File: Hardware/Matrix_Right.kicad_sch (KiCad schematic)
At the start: 125 parts, among them SW38 PG1350, SW39 PG1350, SW40 PG1350, SW41 PG1350, SW42 PG1350, SW43 PG1350, SW44 PG1350, SW45 PG1350, SW46 PG1350, SW47 PG1350, SW48 PG1350, SW49 PG1350, SW50 PG1350, SW51 PG1350, SW52 PG1350, SW53 PG1350, SW54 PG1350, SW55 PG1350, SW56 PG1350, SW57 PG1350, SW58 PG1350, SW59 PG1350, SW60 PG1350, SW61 PG1350, SW62 PG1350, SW63 PG1350, SW64 PG1350, SW65 PG1350, SW66 PG1350, SW67 PG1350, SW68 ENCODER

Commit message: MIP display and LED enable
Return of the LED enable via GPIO.
Changed the TFT display for a MPI panel. It's more expensive than an e-ink one, but the sharpness is really nice.
Need to remove the numbers row to go for a true Corne-ish layout.
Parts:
- renumbered C45 to C47, C46 to C48, C47 to C49, C48 to C50, C49 to C51, C50 to C52, C51 to C53, C52 to C54, C53 to C55, C54 to C56, C55 to C57, C56 to C58, C57 to C59, C58 to C60, C59 to C61, C60 to C62, C61 to C63, C62 to C64, C63 to C65, C64 to C66, C65 to C67, C66 to C68, C67 to C69, C68 to C70, C69 to C71, C70 to C72, C71 to C73, C72 to C74, C73 to C75, C74 to C76, C75 to C77, C76 to C78, D102 to D100, D103 to D101, D104 to D102, D105 to D103, D106 to D104, D107 to D105, D108 to D106, D109 to D107, D110 to D108, D111 to D109, D112 to D110, D113 to D111, D114 to D112, D115 to D113, D116 to D114, D117 to D115, D118 to D116, D119 to D117, D120 to D118, D121 to D119, D122 to D120, D123 to D121, D124 to D122, D125 to D123, D126 to D124, D67 to D65, D68 to D66, D69 to D67, D70 to D68, D71 to D69, D72 to D70, D73 to D71, D74 to D72, D75 to D73, D76 to D74, D77 to D75, D78 to D76, D79 to D77, D80 to D78, D81 to D79, D82 to D80, D83 to D81, D84 to D82, D85 to D83, D86 to D84, D87 to D85, D88 to D86, D89 to D87, D90 to D88, D91 to D89, D92 to D90, D93 to D91, D94 to D92, D95 to D93, D96 to D94, D97 to D95, D98 to D96, D99 to D97, D100 to D98, D101 to D99, R25 to R19, R26 to R20, SW38 to SW36, SW39 to SW37, SW40 to SW38, SW41 to SW39, SW42 to SW40, SW43 to SW41, SW44 to SW42, SW45 to SW43, SW46 to SW44, SW47 to SW45, SW48 to SW46, SW49 to SW47, SW50 to SW48, SW51 to SW49, SW52 to SW50, SW53 to SW51, SW54 to SW52, SW55 to SW53, SW56 to SW54, SW57 to SW55, SW58 to SW56, SW59 to SW57, SW60 to SW58, SW61 to SW59, SW62 to SW60, SW63 to SW61, SW64 to SW62, SW65 to SW63, SW66 to SW64, SW67 to SW65, SW68 to SW66

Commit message: Row removal and key layout
Removed the number row.
Adjusted the spacebar position and changed it to 1u.
Need to consider what to do for one of the halfs if its screen is to be removed.
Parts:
- removed C48, C51, C55, C59, C63, C67: 1u, Capacitor_SMD:C_0603_1608Metric, symbol Device:C
- removed D105, D114, D71, D80, D89, D98: 1N4148WT, Diode_SMD:D_SOD-523, symbol Diode:1N4148WT
- removed D110, D66, D69, D78, D87, D96: SK6812MINI-E, Custom_Parts:LED_SK6812MINI-E_3.2x2.8mm_P1.5mm_ReverseMount, symbol LED:SK6812MINI-E
- removed SW36, SW41, SW46, SW51, SW56, SW61: PG1350, Custom_Parts:PG1350_1.00u_PCB, symbol Switch:SW_Push
- renumbered C76 to C41, C73 to C42, C74 to C43, C72 to C44, C69 to C45, C70 to C46, C68 to C47, C65 to C48, C66 to C49, C64 to C50, C61 to C51, C62 to C52, C60 to C53, C57 to C54, C58 to C55, C53 to C57, C54 to C58, C52 to C59, C49 to C60, C50 to C61, C75 to C62, C71 to C63, C47 to C64, C77 to C65, C78 to C66, D65 to D100, D124 to D53, D121 to D54, D122 to D55, D120 to D56, D112 to D57, D113 to D58, D72 to D59, D73 to D60, D74 to D61, D75 to D62, D111 to D63, D103 to D64, D104 to D65, D81 to D66, D82 to D67, D83 to D68, D84 to D69, D97 to D70, D94 to D71, D95 to D72, D90 to D73, D91 to D74, D92 to D75, D93 to D76, D88 to D77, D99 to D78, D100 to D79, D101 to D80, D102 to D81, D85 to D82, D86 to D83, D79 to D84, D106 to D85, D107 to D86, D108 to D87, D109 to D88, D76 to D89, D77 to D90, D70 to D91, D115 to D92, D116 to D93, D117 to D94, D118 to D95, D67 to D96, D68 to D97, D123 to D98, D119 to D99, SW37 to SW30, SW38 to SW31, SW39 to SW32, SW40 to SW33, SW42 to SW34, SW43 to SW35, SW44 to SW36, SW45 to SW37, SW47 to SW38, SW48 to SW39, SW49 to SW40, SW50 to SW41, SW52 to SW42, SW53 to SW43, SW54 to SW44, SW55 to SW45, SW57 to SW46, SW58 to SW47, SW59 to SW48, SW60 to SW49, SW62 to SW50, SW63 to SW51, SW64 to SW52, SW65 to SW53, SW66 to SW54
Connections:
- net ROW5_R is gone; now on net ROW4_R: D62.1 (K), D69.1 (K), D76.1 (K), D81.1 (K), D88.1 (K), D95.1 (K)
- net LED_DATA_R: now also D54.2 (DIN)
- net ROW1_R: now also D59.1 (K), D66.1 (K), D73.1 (K), D78.1 (K), D85.1 (K), D92.1 (K)
- net ROW2_R: now also D60.1 (K), D67.1 (K), D74.1 (K), D79.1 (K), D86.1 (K), D93.1 (K); no longer D59.1 (K), D66.1 (K), D73.1 (K), D78.1 (K), D85.1 (K), D92.1 (K)
- net ROW3_R: now also D61.1 (K), D68.1 (K), D75.1 (K), D80.1 (K), D87.1 (K), D94.1 (K); no longer D60.1 (K), D67.1 (K), D74.1 (K), D79.1 (K), D86.1 (K), D93.1 (K)
- net ROW4_R: no longer D61.1 (K), D68.1 (K), D75.1 (K), D80.1 (K), D87.1 (K), D94.1 (K)
- net at D96.4 (DOUT): now also D99.2 (DIN); no longer D91.2 (DIN)
- net at D98.4 (DOUT): now also D91.2 (DIN); no longer D54.2 (DIN)
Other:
- moved on the sheet: C41, C42, C43, C44, C45, C46, C47, C48, C49, C50, C51, C52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

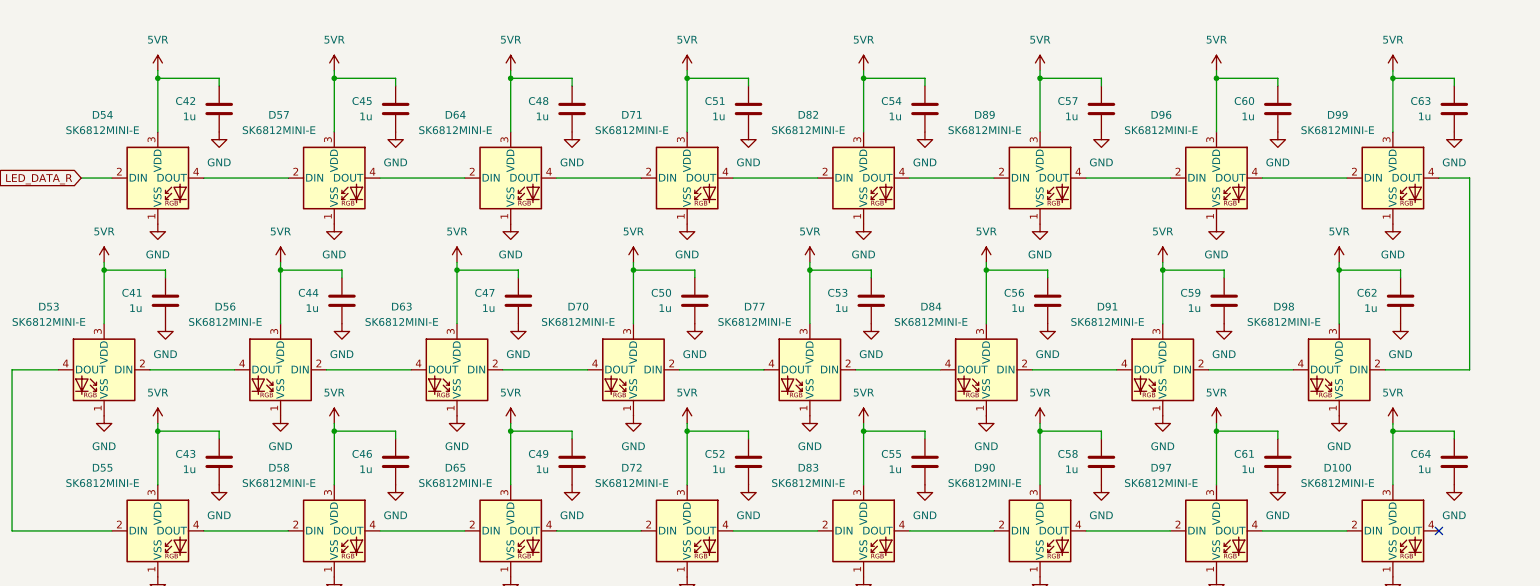
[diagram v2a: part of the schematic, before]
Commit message: Debug connector
Updated the debug connector for a custom one.
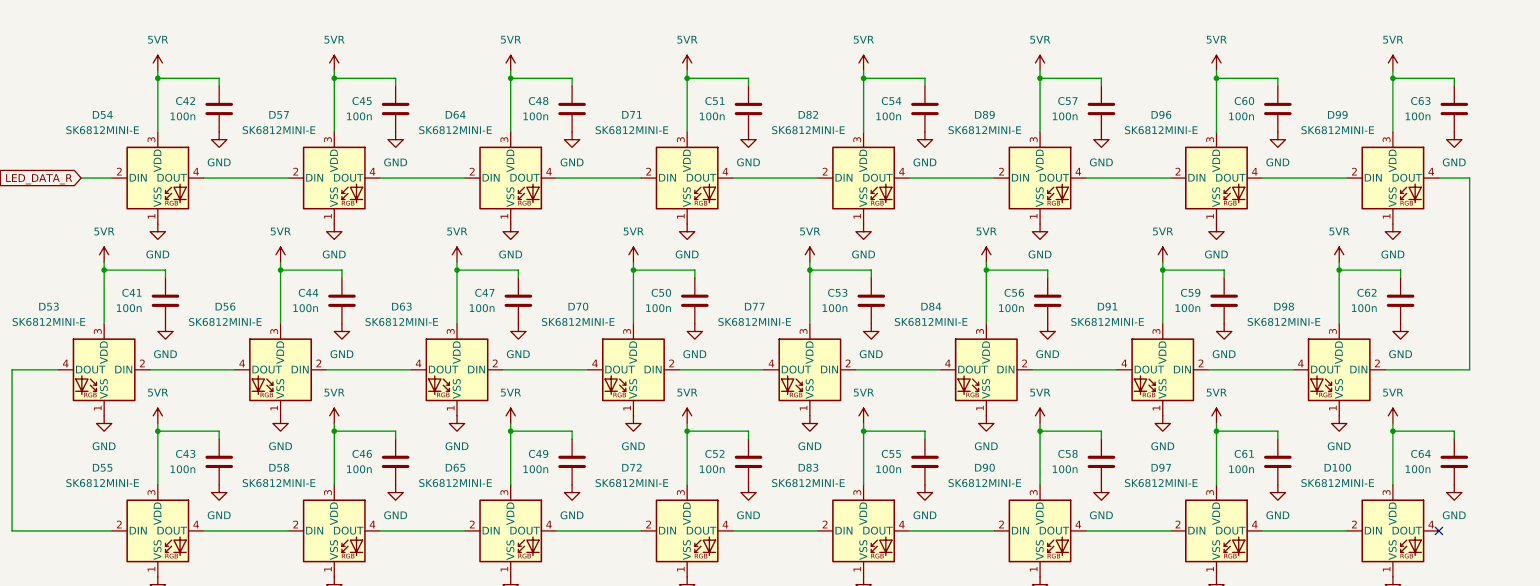
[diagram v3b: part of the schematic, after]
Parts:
- C41, C42, C43, C44, C45, C46, C47, C48, C49, C50, C51, C52, C53, C54, C55, C56, C57, C58, C59, C60, C61, C62, C63, C64: value 1u -> 100n; JLC Part C15849 -> C14663; Manufacturer Part CL10A105KB8NNNC -> CC0603KRX7R9BB104

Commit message: Board outline and routing
Enlarged the board outline by 0.5mm for proper fitment of the switch receptacles.
Updated the footprint for the switch receptacles.
Changed the JTAG connector for a custom one.
Need to review the size of the PCB area dedicated to the MCU and the screen.
Need to consider removing the additional reset button.
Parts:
- SW30, SW31, SW32, SW33, SW34, SW35, SW36, SW37, SW38, SW39, SW40, SW41, SW42, SW43, SW44, SW45, SW46, SW47, SW48, SW49, SW50, SW51, SW52, SW53: footprint Custom_Parts:PG1350_1.00u_PCB -> Custom_Parts:PG1350_1.00u_PCB_TIGHT
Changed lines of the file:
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@@
 			)
 		)
-		(property "Footprint" "Custom_Parts:PG1350_1.00u_PCB"
+		(property "Footprint" "Custom_Parts:PG1350_1.00u_PCB_TIGHT"
 			(at 219.71 102.87 0)
 			(hide yes)
@@
 			)
 		)
-		(property "Footprint" "Custom_Parts:PG1350_1.00u_PCB"
+		(property "Footprint" "Custom_Parts:PG1350_1.00u_PCB_TIGHT"
 			(at 166.37 87.63 0)
 			(hide yes)
@@
 			)
 		)
-		(property "Footprint" "Custom_Parts:PG1350_1.00u_PCB"
+		(property "Footprint" "Custom_Parts:PG1350_1.00u_PCB_TIGHT"
 			(at 113.03 72.39 0)
 			(hide yes)
@@
 			)
 		)
-		(property "Footprint" "Custom_Parts:PG1350_1.00u_PCB"
+		(property "Footprint" "Custom_Parts:PG1350_1.00u_PCB_TIGHT"
 			(at 113.03 57.15 0)
 			(hide yes)
@@
 			)
 		)
-		(property "Footprint" "Custom_Parts:PG1350_1.00u_PCB"
+		(property "Footprint" "Custom_Parts:PG1350_1.00u_PCB_TIGHT"
 			(at 166.37 102.87 0)
 			(hide yes)
@@
 			)
 		)
-		(property "Footprint" "Custom_Parts:PG1350_1.00u_PCB"
+		(property "Footprint" "Custom_Parts:PG1350_1.00u_PCB_TIGHT"
 			(at 139.7 72.39 0)
 			(hide yes)
@@
 			)
 		)
-		(property "Footprint" "Custom_Parts:PG1350_1.00u_PCB"
+		(property "Footprint" "Custom_Parts:PG1350_1.00u_PCB_TIGHT"
 			(at 219.71 72.39 0)
 			(hide yes)
@@
 			)
 		)
-		(property "Footprint" "Custom_Parts:PG1350_1.00u_PCB"
+		(property "Footprint" "Custom_Parts:PG1350_1.00u_PCB_TIGHT"
 			(at 139.7 87.63 0)
 			(hide yes)
@@
 			)
 		)
-		(property "Footprint" "Custom_Parts:PG1350_1.00u_PCB"
+		(property "Footprint" "Custom_Parts:PG1350_1.00u_PCB_TIGHT"
 			(at 86.36 72.39 0)
 			(hide yes)
@@
 			)
 		)
-		(property "Footprint" "Custom_Parts:PG1350_1.00u_PCB"
+		(property "Footprint" "Custom_Parts:PG1350_1.00u_PCB_TIGHT"
 			(at 193.04 87.63 0)
 			(hide yes)
@@
 			)
 		)
-		(property "Footprint" "Custom_Parts:PG1350_1.00u_PCB"
+		(property "Footprint" "Custom_Parts:PG1350_1.00u_PCB_TIGHT"
 			(at 193.04 72.39 0)
 			(hide yes)
@@
 			)
 		)
-		(property "Footprint" "Custom_Parts:PG1350_1.00u_PCB"
+		(property "Footprint" "Custom_Parts:PG1350_1.00u_PCB_TIGHT"
 			(at 139.7 102.87 0)
 			(hide yes)
@@
 			)
 		)
-		(property "Footprint" "Custom_Parts:PG1350_1.00u_PCB"
+		(property "Footprint" "Custom_Parts:PG1350_1.00u_PCB_TIGHT"
 			(at 113.03 102.87 0)
 			(hide yes)
@@
 			)
 		)
-		(property "Footprint" "Custom_Parts:PG1350_1.00u_PCB"
+		(property "Footprint" "Custom_Parts:PG1350_1.00u_PCB_TIGHT"
 			(at 219.71 57.15 0)
 			(hide yes)
@@
 			)
 		)
-		(property "Footprint" "Custom_Parts:PG1350_1.00u_PCB"
+		(property "Footprint" "Custom_Parts:PG1350_1.00u_PCB_TIGHT"
 			(at 86.36 102.87 0)
 			(hide yes)
@@
 			)
 		)
-		(property "Footprint" "Custom_Parts:PG1350_1.00u_PCB"
+		(property "Footprint" "Custom_Parts:PG1350_1.00u_PCB_TIGHT"
 			(at 166.37 72.39 0)
 			(hide yes)
@@
 			)
 		)
-		(property "Footprint" "Custom_Parts:PG1350_1.00u_PCB"
+		(property "Footprint" "Custom_Parts:PG1350_1.00u_PCB_TIGHT"
 			(at 139.7 57.15 0)
 			(hide yes)
@@
 			)
 		)
-		(property "Footprint" "Custom_Parts:PG1350_1.00u_PCB"
+		(property "Footprint" "Custom_Parts:PG1350_1.00u_PCB_TIGHT"
 			(at 166.37 57.15 0)
 			(hide yes)
@@
 			)
 		)
-		(property "Footprint" "Custom_Parts:PG1350_1.00u_PCB"
+		(property "Footprint" "Custom_Parts:PG1350_1.00u_PCB_TIGHT"
 			(at 193.04 57.15 0)
 			(hide yes)
@@
 			)
 		)
-		(property "Footprint" "Custom_Parts:PG1350_1.00u_PCB"
+		(property "Footprint" "Custom_Parts:PG1350_1.00u_PCB_TIGHT"
 			(at 193.04 102.87 0)
 			(hide yes)
@@
 			)
 		)
-		(property "Footprint" "Custom_Parts:PG1350_1.00u_PCB"
+		(property "Footprint" "Custom_Parts:PG1350_1.00u_PCB_TIGHT"
 			(at 86.36 87.63 0)
 			(hide yes)
@@
 			)
 		)
-		(property "Footprint" "Custom_Parts:PG1350_1.00u_PCB"
+		(property "Footprint" "Custom_Parts:PG1350_1.00u_PCB_TIGHT"
 			(at 86.36 57.15 0)
 			(hide yes)
@@
 			)
 		)
-		(property "Footprint" "Custom_Parts:PG1350_1.00u_PCB"
+		(property "Footprint" "Custom_Parts:PG1350_1.00u_PCB_TIGHT"
 			(at 113.03 87.63 0)
 			(hide yes)
@@
 			)
 		)
-		(property "Footprint" "Custom_Parts:PG1350_1.00u_PCB"
+		(property "Footprint" "Custom_Parts:PG1350_1.00u_PCB_TIGHT"
 			(at 219.71 87.63 0)
 			(hide yes)

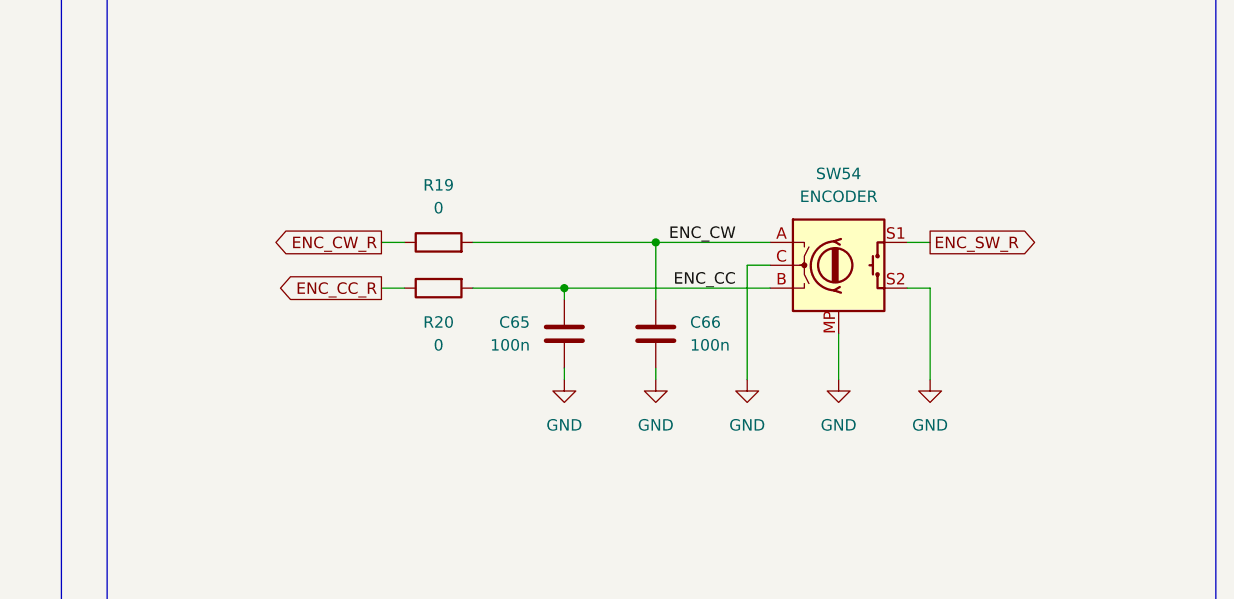
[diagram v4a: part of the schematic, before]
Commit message: Matrix routing and data lines
Routed some of the lines for the switch matrix.
Routed the singal lines for the MIP display.
Need to check clearenaces and spacing between the SPI lines.
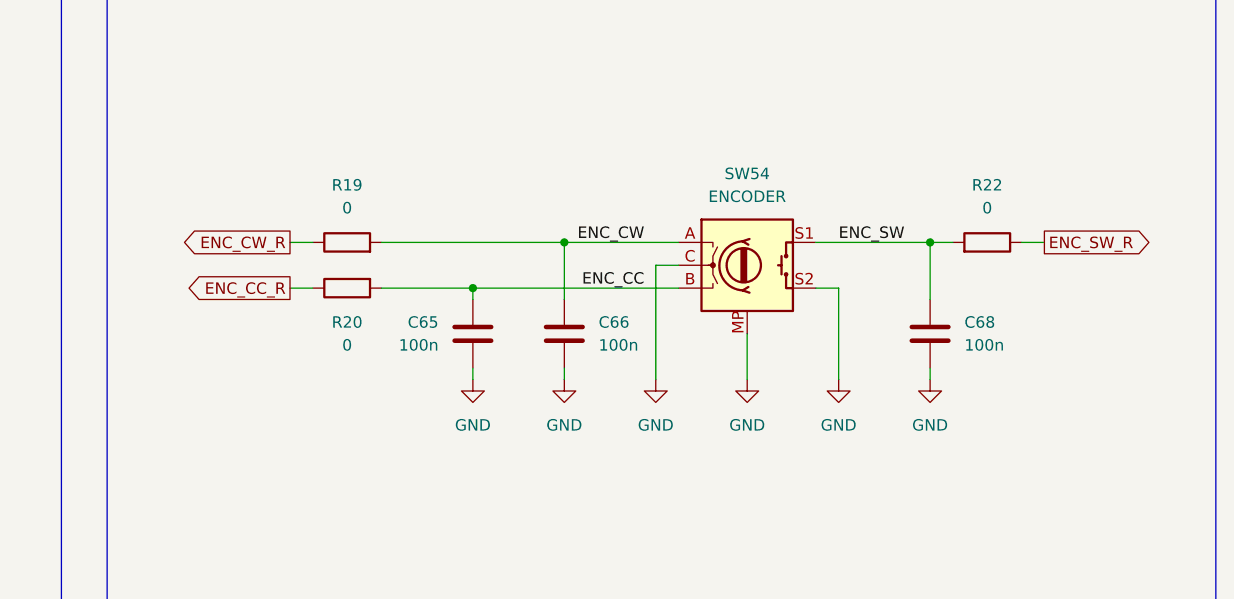
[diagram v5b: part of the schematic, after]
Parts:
- added C68: 100n, Capacitor_SMD:C_0603_1608Metric, symbol Device:C
- added R22: 0, Resistor_SMD:R_0603_1608Metric, symbol Device:R
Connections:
- net ENC_SW_R: now also R22.1; no longer SW54.S1
- net GND: now also C68.2
- new net ENC_SW: C68.1, R22.2, SW54.S1
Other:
- moved on the sheet: C65, C66, R19, R20, SW54
